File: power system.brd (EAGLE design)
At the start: 92.4 x 94 mm, 43 parts

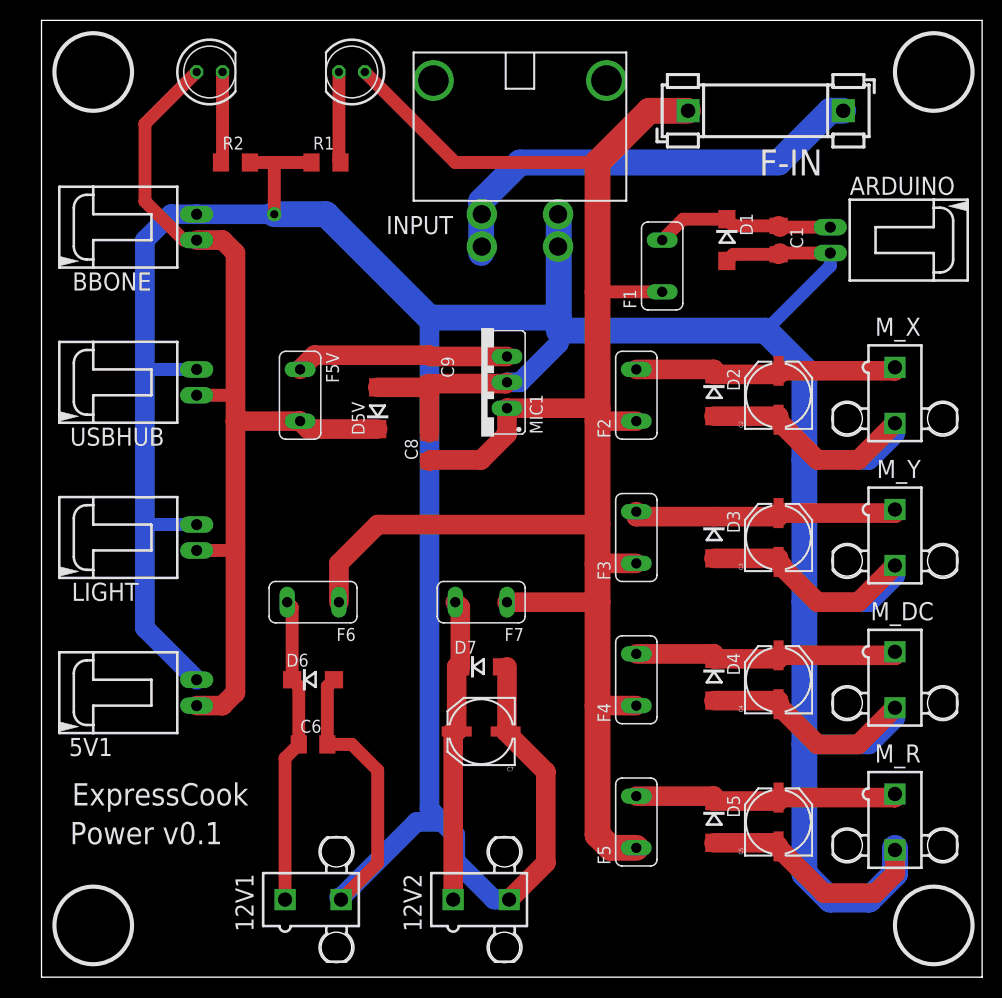
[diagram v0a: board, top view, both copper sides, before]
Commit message: 1. increase the wire width 2. merge the two brd file 3. change the fuse value and connector order 4. approve the DRC error
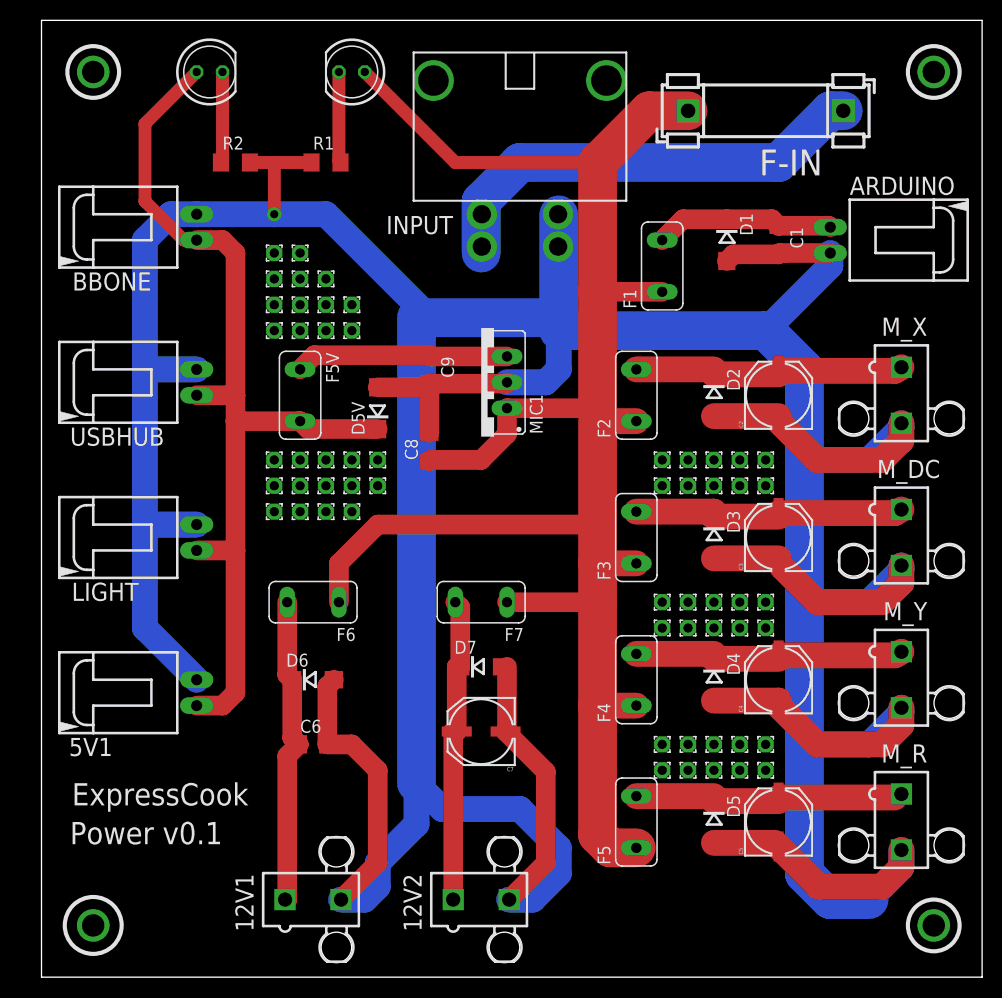
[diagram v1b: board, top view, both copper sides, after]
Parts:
- added E$1, E$10, E$11, E$12, E$13, E$14, E$15, E$16, E$17, E$18, E$19, E$2, E$20, E$21, E$22, E$23, E$24, E$25, E$26, E$27, E$28, E$29, E$3, E$30, E$31, E$32, E$33, E$34, E$35, E$36, E$37, E$38, E$39, E$4, E$40, E$41, E$42, E$43, E$44, E$45, E$46, E$47, E$48, E$49, E$5, E$50, E$51, E$52, E$53, E$54, E$55, E$56, E$57, E$6, E$7, E$8, E$9: (no value), wirepad:1,6/0,9
- F2, F3: value 3A -> 4A
- F4: value 4A -> 2A
- moved M_DC 14.0 mm to (83.2, 35.6)
- moved M_Y 14.0 mm to (83.2, 21.6)
- moved M_R 0.64 mm to (83.2, 7.62)
- moved M_X 0.64 mm to (83.2, 49.5)
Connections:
- net N$12: now also M_Y.1; no longer M_DC.1
- net N$6: now also M_DC.1; no longer M_Y.1
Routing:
- net GND: track 507.4 -> 527.9 mm
- net N$15: track 27.0 -> 27.6 mm

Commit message: increas track to 20
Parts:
- removed E$23, E$28, E$29, E$47, E$56, E$57: (no value), wirepad:1,6/0,9
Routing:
- net GND: track 527.9 -> 554.5 mm
- net N$8: track 185.5 -> 194.3 mm
- net N$3: track 44.3 -> 46.9 mm
